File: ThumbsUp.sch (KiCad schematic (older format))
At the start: 159 parts, among them J19 52559-1233, J32 Battery, SW2 SW_DIP_x01, U1 ProMicro

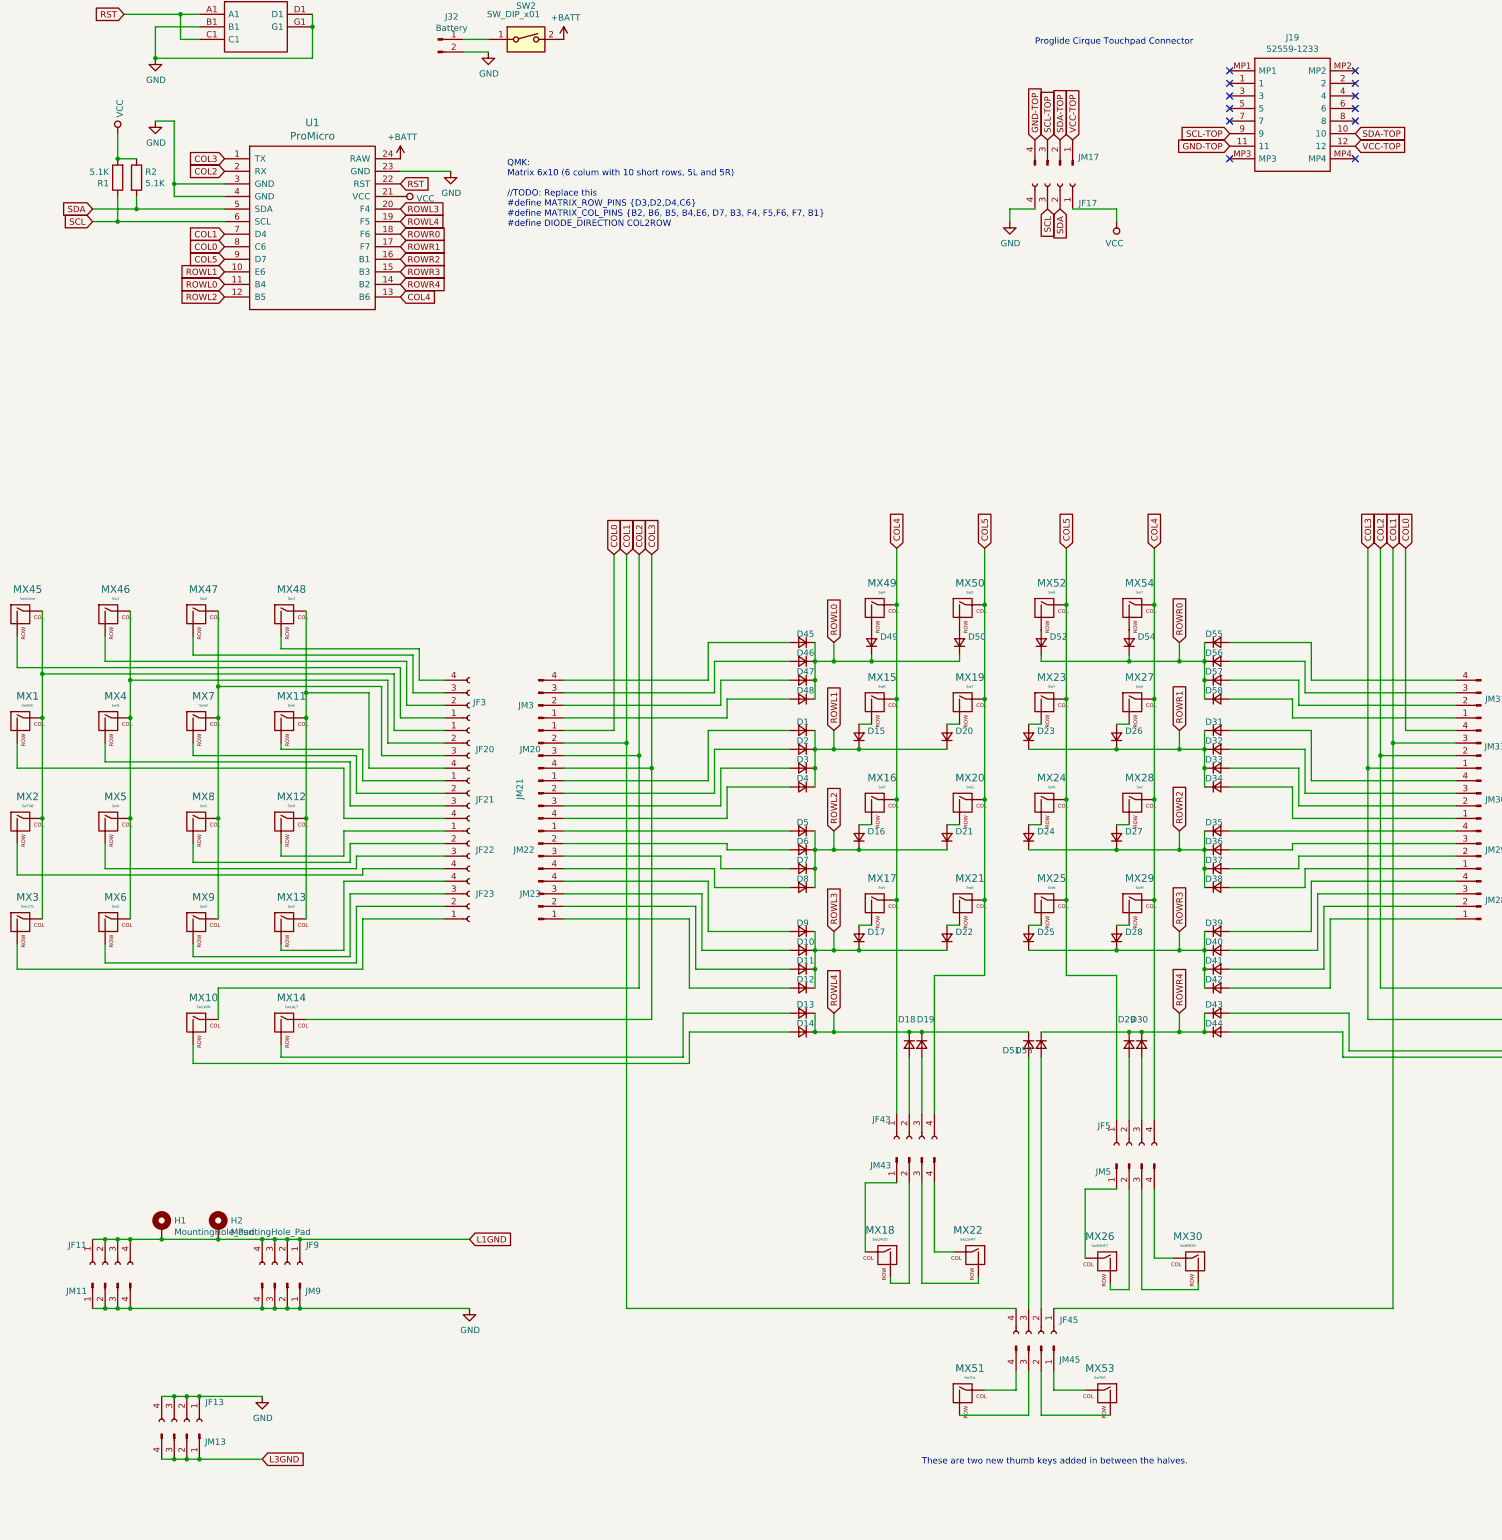
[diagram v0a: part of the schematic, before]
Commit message: Updated the schematics, replaced the switches with MX/Kailh Choc combo
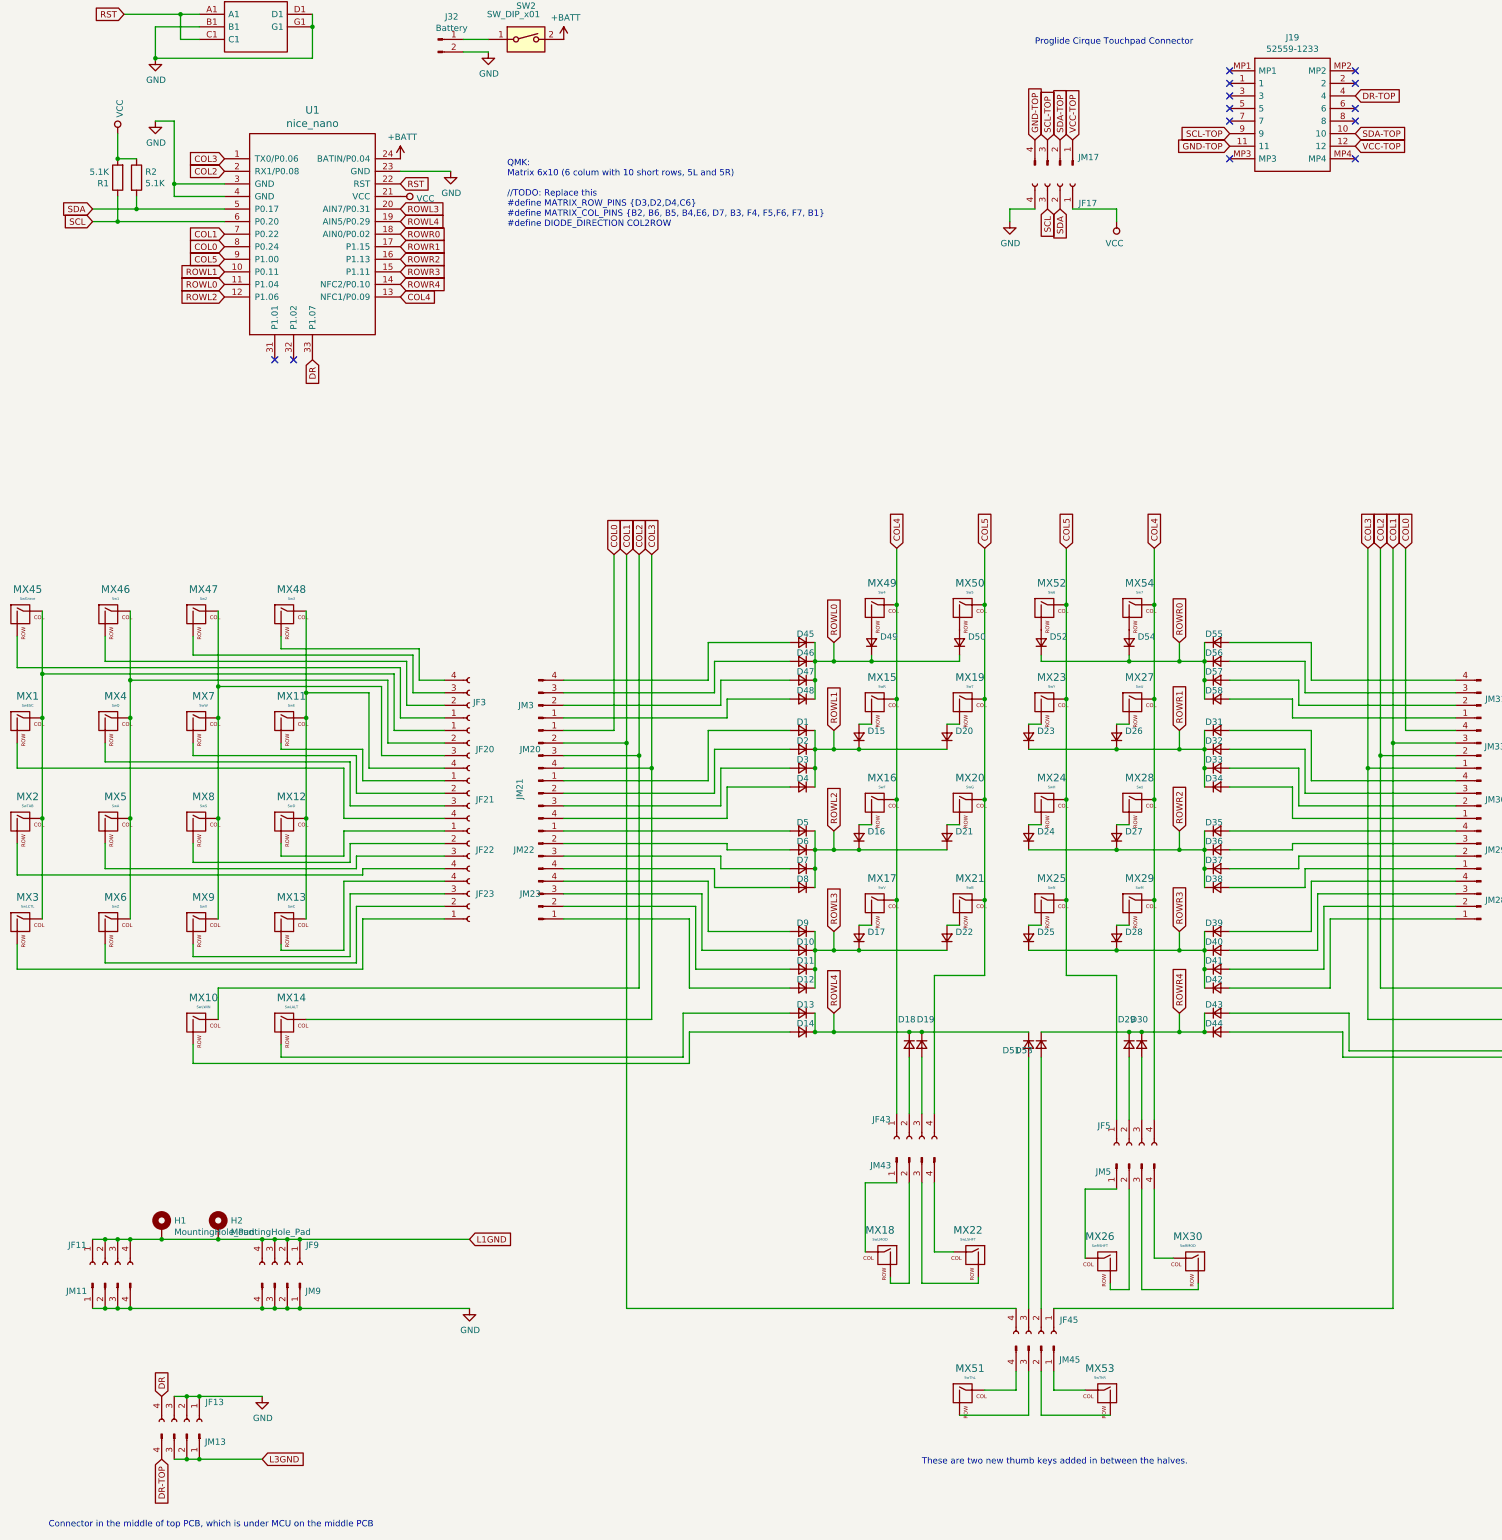
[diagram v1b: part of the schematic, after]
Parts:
- removed U1: ProMicro, promicro:ProMicro, symbol promicro:ProMicro
- added U1: nice_nano, nice-nano-kicad:nice_nano, symbol nice_nano:nice_nano
- MX1, MX10, MX11, MX12, MX13, MX14, MX15, MX16, MX17, MX18, MX19, MX2, MX20, MX21, MX22, MX23, MX24, MX25, MX26, MX27, MX28, MX29, MX3, MX30, MX31, MX32, MX33, MX34, MX35, MX36, MX37, MX38, MX39, MX4, MX40, MX41, MX42, MX43, MX44, MX45, MX46, MX47, MX48, MX49, MX5, MX50, MX51, MX52, MX53, MX54, MX55, MX56, MX57, MX58, MX6, MX7, MX8, MX9: footprint keyswitches:PG1350_GLv2 -> keyswitches:PG1350_MX_sockets
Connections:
- net +BATT: now also U1.24 (BATIN/P0.04)
- net COL0: now also U1.8 (P0.24)
- net COL1: now also U1.7 (P0.22)
- net COL2: now also U1.2 (RX1/P0.08)
- net COL3: now also U1.1 (TX0/P0.06)
- net COL4: now also U1.13 (NFC1/P0.09)
- net COL5: now also U1.9 (P1.00)
- net GND: now also U1.23 (GND), U1.3 (GND), U1.4 (GND); no longer JF13.4 (Pin_4)
- net L3GND: no longer JM13.4 (Pin_4)
- net ROWL0: now also U1.11 (P1.04)
- net ROWL1: now also U1.10 (P0.11)
- net ROWL2: now also U1.12 (P1.06)
- net ROWL3: now also U1.20 (AIN7/P0.31)
- net ROWL4: now also U1.19 (AIN5/P0.29)
- net ROWR0: now also U1.18 (AIN0/P0.02)
- net ROWR1: now also U1.17 (P1.15)
- net ROWR2: now also U1.16 (P1.13)
- net ROWR3: now also U1.15 (P1.11)
- net ROWR4: now also U1.14 (NFC2/P0.10)
- net RST: now also U1.22 (RST)
- net SCL: now also U1.6 (P0.20)
- net SDA: now also U1.5 (P0.17)
- net VCC: now also U1.21 (VCC)
- net DR-TOP: now reaches J19.4
- net DR-TOP: now also JM13.4 (Pin_4)
- new net DR: JF13.4 (Pin_4), U1.33 (P1.07)
- no-connect marks 13 -> 14
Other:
- note added: "Connector in the middle of top PCB, which is under MCU on the middle PCB"
